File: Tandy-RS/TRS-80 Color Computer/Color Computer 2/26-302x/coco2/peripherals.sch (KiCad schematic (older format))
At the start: 0 parts

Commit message: -Added video sheet -moved salt chip from power sheet to peripheral sheet
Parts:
- added C11, C5: 100uF 16v, Capacitor_THT:CP_Radial_D8.0mm_P5.00mm, symbol Device:CP_Small
- added C2: 4700uF 16V, Capacitor_THT:CP_Radial_D16.0mm_P7.50mm, symbol Device:CP_Small
- added C6: .1uF, Capacitor_THT:C_Axial_L3.8mm_D2.6mm_P10.00mm_Horizontal, symbol Device:C_Small
- added J5: Conn_01x16_Female, Connector_PinHeader_2.54mm:PinHeader_1x15_P2.54mm_Vertical, symbol Connector:Conn_01x16_Female
- added Q1: 2N3055, Package_TO_SOT_THT:TO-3, symbol Transistor_BJT:2N3055
- added R1: 51, Resistor_THT:R_Axial_DIN0207_L6.3mm_D2.5mm_P10.16mm_Horizontal, symbol Device:R_Small_US
- added R2: .1 ohms 1/2W, Resistor_THT:R_Axial_DIN0411_L9.9mm_D3.6mm_P20.32mm_Horizontal, symbol Device:R_Small_US
- added U1: SC77527P, Package_DIP:DIP-16_W7.62mm, symbol coco2:SC77527P
- added U2: 6821, Package_DIP:DIP-40_W15.24mm, symbol Interface:6821
- added U3: SC77526, Package_DIP:DIP-20_W7.62mm, symbol custom_dac:SC77526
- added U7: 6822, Package_DIP:DIP-40_W15.24mm, symbol Interface:6822
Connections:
- new net: Q1.1 (B), U1.1 (PASS_TRANS_BASE_DRIVE)
- new net: Q1.2 (E), R1.1, R2.2
- new net: R1.2, U1.2 (PASS_TRANS_SENSE)
- new net: J5.9 (Pin_9), U7.10 (PB0)
- new net: J5.10 (Pin_10), U7.11 (PB1)
- new net: J5.11 (Pin_11), U7.12 (PB2)
- new net: J5.12 (Pin_12), U7.13 (PB3)
- new net: J5.13 (Pin_13), U7.14 (PB4)
- new net: J5.14 (Pin_14), U7.15 (PB5)
- new net: J5.15 (Pin_15), U7.16 (PB6)
- new net: J5.16 (Pin_16), U7.17 (PB7)
- new net: J5.1 (Pin_1), U7.2 (PA0)
- new net: J5.2 (Pin_2), U7.3 (PA1)
- new net: J5.3 (Pin_3), U7.4 (PA2)
- new net: J5.4 (Pin_4), U7.5 (PA3)
- new net: J5.5 (Pin_5), U7.6 (PA4)
- new net: J5.6 (Pin_6), U7.7 (PA5)
- new net: J5.7 (Pin_7), U7.8 (PA6)
- new net: J5.8 (Pin_8), U7.9 (PA7)
- new net +5V: C11.1, C5.1, C6.2, R2.1, U1.3 (CURRENT_LIMT), U7.20 (VCC)
- new net +SALT_VIN: U1.15 (UN_REG_-V_IN)
- new net -SALT_VIN: C2.1, Q1.3 (C), U1.16 (UN_REG_+V_IN)
- new net D0: U7.33 (D0)
- new net D1: U7.32 (D1)
- new net D2: U7.31 (D2)
- new net D3: U7.30 (D3)
- new net D4: U7.29 (D4)
- new net D5: U7.28 (D5)
- new net D6: U7.27 (D6)
- new net D7: U7.26 (D7)
- new net GNDS: C11.2, C2.2, C5.2, C6.1, U1.8 (GND), U7.1 (VSS)
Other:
- note added: "The SALT chip (Supply and Level Translator)"
- note added: "http://roust-it.dk/coco/coco2_service_manual.pdf"
- note added: "interface level translation, cassette read"
- note added: "is responsible for supply regulation, RS-232"
- note added: "operations, and driving the cassette relay."

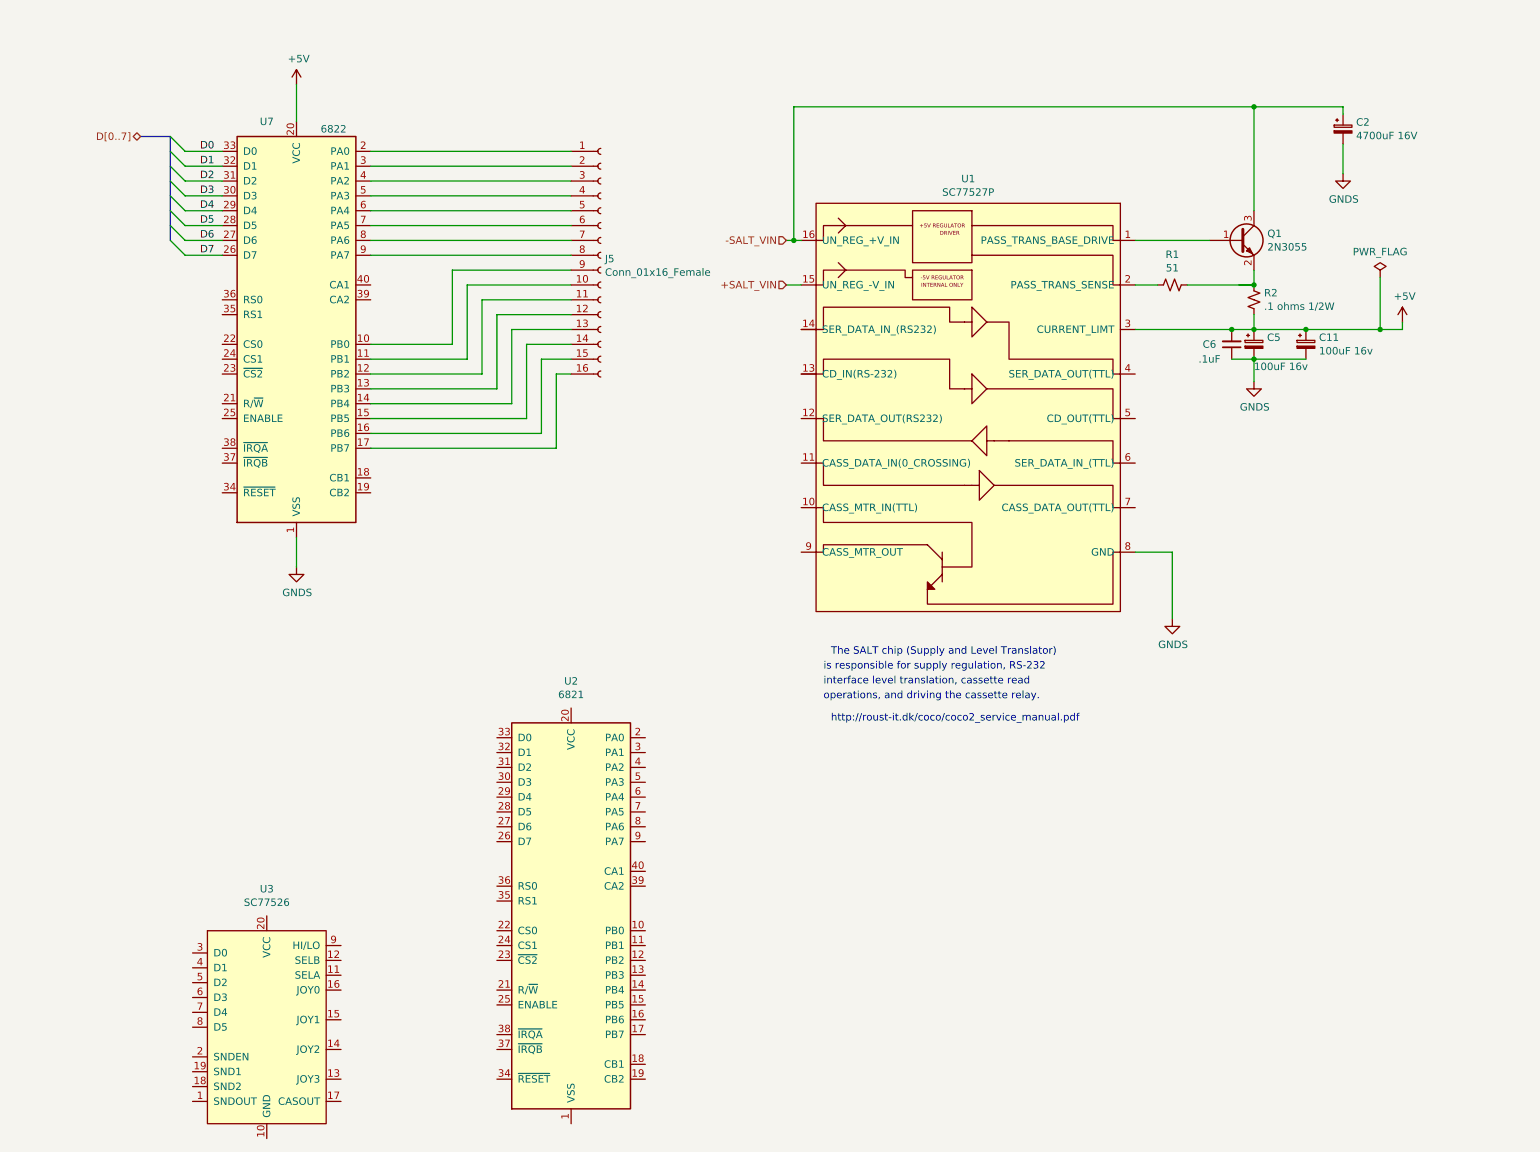
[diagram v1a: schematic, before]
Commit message: Added some more stuff to the perhipherals  sheet
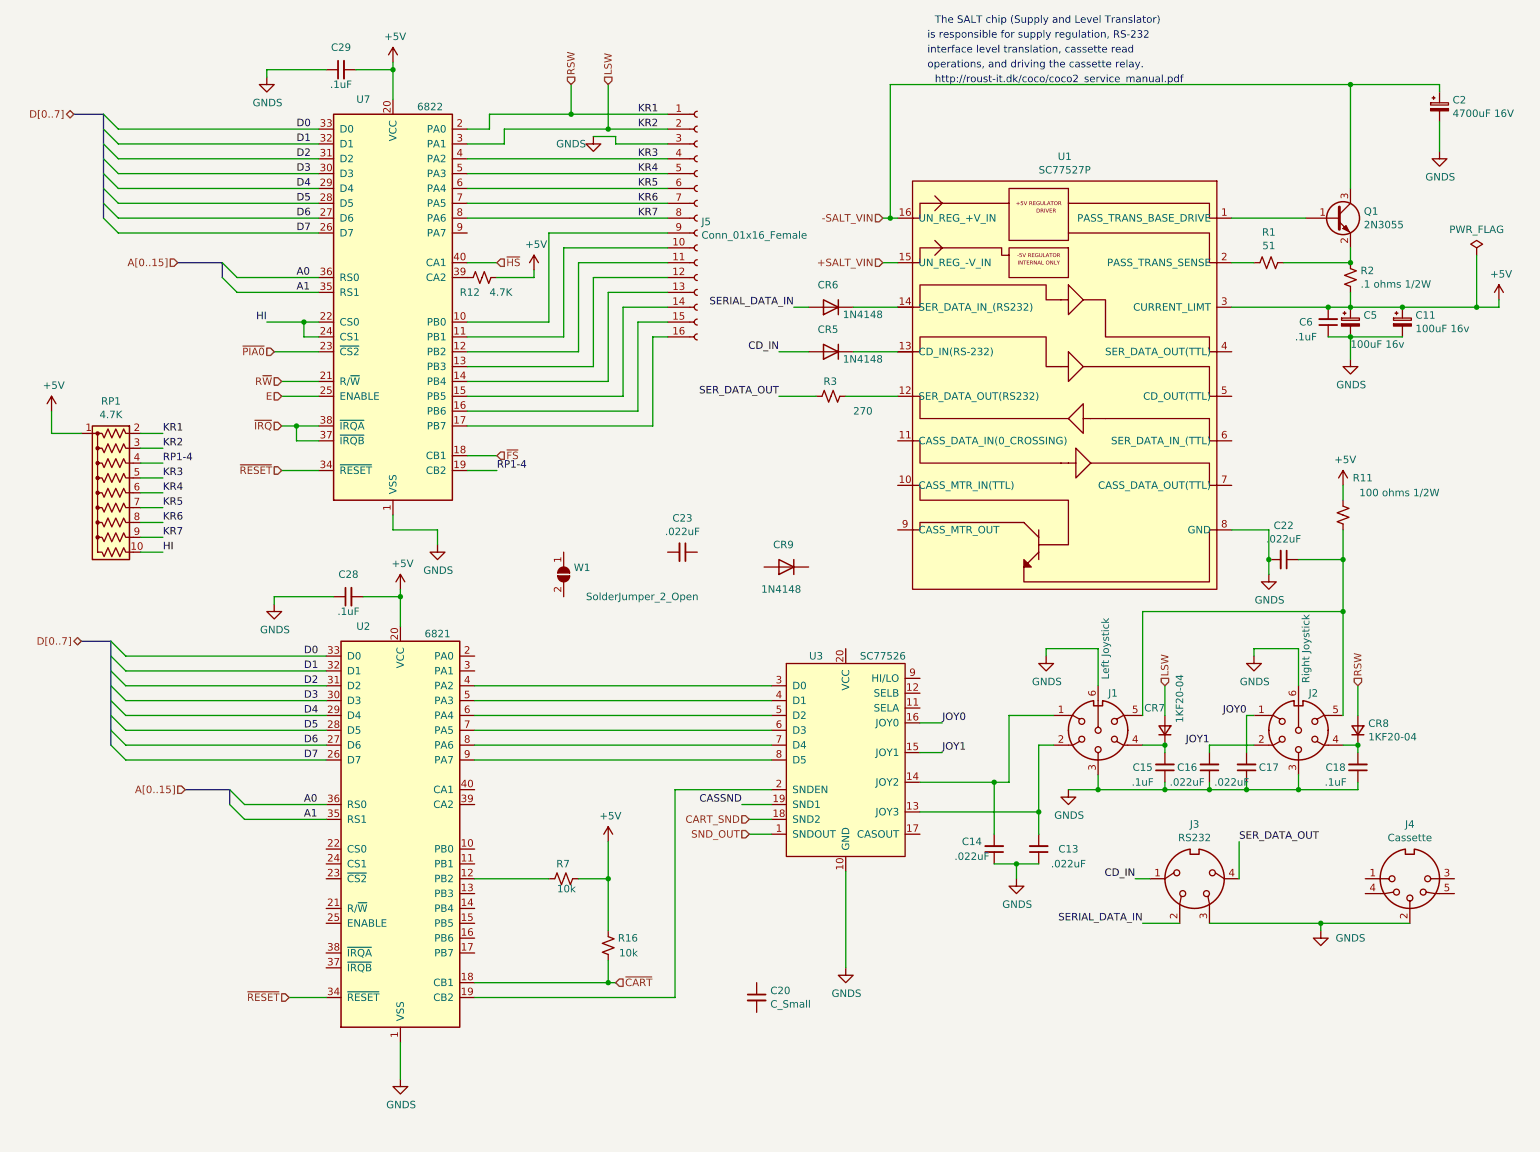
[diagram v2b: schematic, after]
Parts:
- added C13, C14, C16, C17, C22, C23: .022uF, Capacitor_THT:C_Disc_D8.0mm_W5.0mm_P5.00mm, symbol Device:C_Small
- added C15, C18, C28, C29: .1uF, Capacitor_THT:C_Axial_L3.8mm_D2.6mm_P10.00mm_Horizontal, symbol Device:C_Small
- added C20: C_Small, Capacitor_THT:CP_Radial_D5.0mm_P2.50mm, symbol Device:C_Small
- added CR5, CR6, CR9: 1N4148, Diode_THT:D_DO-35_SOD27_P7.62mm_Horizontal, symbol Diode:1N4148
- added CR7, CR8: 1KF20-04, Diode_THT:D_DO-15_P15.24mm_Horizontal, symbol Device:D_Small
- added J1: Left Joystick, coco2:CUI_SDS-60J, symbol Connector:DIN-6
- added J2: Right Joystick, coco2:CUI_SDS-60J, symbol Connector:DIN-6
- added J3: RS232, coco2:CUI_SDS-40J, symbol Connector:DIN-4
- added J4: Cassette, coco2:CUI_SDS-50J, symbol Connector:DIN-5_180degree
- added R11: 100 ohms 1/2W, Resistor_THT:R_Axial_DIN0411_L9.9mm_D3.6mm_P20.32mm_Horizontal, symbol Device:R_Small_US
- added R12: 4.7K, Resistor_THT:R_Axial_DIN0207_L6.3mm_D2.5mm_P10.16mm_Horizontal, symbol Device:R_Small_US
- added R16, R7: 10k, Resistor_THT:R_Axial_DIN0207_L6.3mm_D2.5mm_P10.16mm_Horizontal, symbol Device:R_Small_US
- added R3: 270, Resistor_THT:R_Axial_DIN0207_L6.3mm_D2.5mm_P10.16mm_Horizontal, symbol Device:R_Small_US
- added RP1: 4.7K, Resistor_THT:R_Array_SIP10, symbol Device:R_Network09_US
- added W1: SolderJumper_2_Open, Jumper:SolderJumper-2_P1.3mm_Open_RoundedPad1.0x1.5mm, symbol Jumper:SolderJumper_2_Open
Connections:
- net +5V: now also U2.20 (VCC), C28.2, C29.2, R11.1, R12.1, R16.2, R7.1, RP1.1 (common)
- net D0: now also U2.33 (D0)
- net D1: now also U2.32 (D1)
- net D2: now also U2.31 (D2)
- net D3: now also U2.30 (D3)
- net D4: now also U2.29 (D4)
- net D5: now also U2.28 (D5)
- net D6: now also U2.27 (D6)
- net D7: now also U2.26 (D7)
- net GNDS: now also J5.3 (Pin_3), U2.1 (VSS), U3.10 (GND), C13.1, C14.1, C15.1, C16.1, C17.1, C18.1, C22.2, C28.1, C29.1, J1.3, J1.6, J2.3, J2.6, J3.3, J4.2
- net at U1.12 (SER_DATA_OUT(RS232)): now also R3.1
- net at U1.13 (CD_IN(RS-232)): now also CR5.1 (K)
- net at U1.14 (SER_DATA_IN_(RS232)): now also CR6.1 (K)
- net at U2.12 (PB2): now also R7.2
- net ~CART: now reaches U2.18 (CB1)
- net ~CART: now also R16.1
- net at U2.19 (CB2): now also U3.2 (SNDEN)
- net ~RESET: now reaches U2.34 (~RESET)
- net ~RESET: now also U7.34 (~RESET)
- net A1: now reaches U2.35 (RS1)
- net A1: now also U7.35 (RS1)
- net A0: now reaches U2.36 (RS0)
- net A0: now also U7.36 (RS0)
- net at U2.4 (PA2): now also U3.3 (D0)
- net at U2.5 (PA3): now also U3.4 (D1)
- net at U2.6 (PA4): now also U3.5 (D2)
- net at U2.7 (PA5): now also U3.6 (D3)
- net at U2.8 (PA6): now also U3.7 (D4)
- net at U2.9 (PA7): now also U3.8 (D5)
- net SND_OUT: now reaches U3.1 (SNDOUT)
- net at U3.13 (JOY3): now also C13.2, J1.2
- net at U3.14 (JOY2): now also C14.2, J1.1
- net JOY1: now reaches U3.15 (JOY1)
- net JOY1: now also C16.2, J2.2
- net JOY0: now reaches U3.16 (JOY0)
- net JOY0: now also C17.2, J2.1
- net CART_SND: now reaches U3.18 (SND2)
- net CASSND: now reaches U3.19 (SND1)
- net ~FS: now reaches U7.18 (CB1)
- net RP1-4: now reaches U7.19 (CB2)
- net RP1-4: now also RP1.4 (R3)
- net RSW: now reaches J5.1 (Pin_1), U7.2 (PA0)
- net RSW: now also CR8.2 (A), RP1.2 (R1)
- net R~W: now reaches U7.21 (R/~W)
- net HI: now reaches U7.22 (CS0)
- net HI: now also U7.24 (CS1), RP1.10 (R9)
- net ~PIA0: now reaches U7.23 (~CS2)
- net E: now reaches U7.25 (ENABLE)
- net LSW: now reaches J5.2 (Pin_2), U7.3 (PA1)
- net LSW: now also CR7.2 (A), RP1.3 (R2)
- net ~IRQ: now reaches U7.37 (~IRQB)
- net ~IRQ: now also U7.38 (~IRQA)
- net at U7.39 (CA2): now also R12.2
- net KR3: now reaches U7.4 (PA2)
- net KR3: now also J5.4 (Pin_4), RP1.5 (R4); no longer J5.3 (Pin_3)
- net ~HS: now reaches U7.40 (CA1)
- net KR4: now reaches U7.5 (PA3)
- net KR4: now also J5.5 (Pin_5), RP1.6 (R5); no longer J5.4 (Pin_4)
- net KR5: now reaches U7.6 (PA4)
- net KR5: now also J5.6 (Pin_6), RP1.7 (R6); no longer J5.5 (Pin_5)
- net KR6: now reaches U7.7 (PA5)
- net KR6: now also J5.7 (Pin_7), RP1.8 (R7); no longer J5.6 (Pin_6)
- net KR7: now reaches U7.8 (PA6)
- net KR7: now also J5.8 (Pin_8), RP1.9 (R8); no longer J5.7 (Pin_7)
- net at U7.9 (PA7): no longer J5.8 (Pin_8)
- new net: C15.2, CR7.1 (K), J1.4
- new net: C22.1, J1.5, J2.5, R11.2
- new net: C18.2, CR8.1 (K), J2.4
- new net CD_IN: CR5.2 (A), J3.1
- new net SERIAL_DATA_IN: CR6.2 (A), J3.2
- new net SER_DATA_OUT: J3.4, R3.2
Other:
- moved on the sheet: C11, C2, C5, C6, J5, Q1, R1, R2, U1, U2, U3, U7

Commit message: Finished peripherals sheet. I think......
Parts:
- added C60: 33pF, Capacitor_THT:C_Rect_L7.2mm_W3.0mm_P5.00mm_FKS2_FKP2_MKS2_MKP2, symbol Device:C_Small
- added K1: HB1-DC5V-H62, coco2:HB1-DC5V-H62_W7.62mm, symbol coco2:HB1-DC5V-H62
- added R23: 220 1/2W, Resistor_THT:R_Axial_DIN0411_L9.9mm_D3.6mm_P20.32mm_Horizontal, symbol Device:R_Small_US
- added R4: 510, Resistor_THT:R_Axial_DIN0207_L6.3mm_D2.5mm_P10.16mm_Horizontal, symbol Device:R_Small_US
- added R8: 10k, Resistor_THT:R_Axial_DIN0207_L6.3mm_D2.5mm_P10.16mm_Horizontal, symbol Device:R_Small_US
- C20: value C_Small -> 10uF NP
- R11: value 100 ohms 1/2W -> 100 1/2W
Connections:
- net CASSND is gone; now on an unnamed net: U3.19 (SND1)
- net +5V: now also CR9.1 (K), R12.2, K1.2 (+); no longer R12.1
- net E: now also U2.25 (ENABLE), C60.2
- net GNDS: now also C23.1, C60.1, R23.1
- net HI: now also U2.22 (CS0), U2.24 (CS1)
- net RP1-4: now also U3.12 (SELB)
- net R~W: now also U2.21 (R/~W)
- net SND_OUT: now also R8.1
- net CASS_M_IN_TTL: now reaches U1.10 (CASS_MTR_IN(TTL))
- net CASS_M_IN_TTL: now also U2.39 (CA2)
- net at U1.11 (CASS_DATA_IN(0_CROSSING)): now also R4.2
- net SER_DATA_OUT_TTL: now reaches U1.4 (SER_DATA_OUT(TTL))
- net SER_DATA_OUT_TTL: now also U2.10 (PB0)
- net CD_OUT_TTL: now reaches U1.5 (CD_OUT(TTL))
- net CD_OUT_TTL: now also U2.40 (CA1)
- net SER_DATA_IN_TTL: now reaches U1.6 (SER_DATA_IN_(TTL))
- net SER_DATA_IN_TTL: now also U2.3 (PA1)
- net CASS_DATA_OUT_TTL: now reaches U1.7 (CASS_DATA_OUT(TTL))
- net CASS_DATA_OUT_TTL: now also U2.2 (PA0)
- net CASS_MTR_OUT: now reaches U1.9 (CASS_MTR_OUT)
- net CASS_MTR_OUT: now also CR9.2 (A), K1.8 (-)
- net at U2.11 (PB1): now also R8.2
- net at R7.2, U2.12 (PB2): now also W1.2 (B)
- net CSS: now reaches U2.13 (PB3)
- net ~INT~_EXT: now reaches U2.14 (PB4)
- net GM1: now reaches U2.15 (PB5)
- net GM2: now reaches U2.16 (PB6)
- net ~A~_G: now reaches U2.17 (PB7)
- net ~CS_PIA1: now reaches U2.23 (~CS2)
- net ~FIRQ: now reaches U2.37 (~IRQB)
- net ~FIRQ: now also U2.38 (~IRQA)
- net SELA: now reaches U3.11 (SELA)
- net SELA: now also R12.1, U7.39 (CA2)
- net CASSOUT: now reaches U3.17 (CASOUT)
- net CASSOUT: now also J4.5
- net HI_LO: now reaches U3.9 (HI/LO)
- net HI_LO: now also U7.9 (PA7)
- net at J5.15 (Pin_15), U7.16 (PB6): now also W1.1 (A)
- net CASS_DATA_IN: now reaches C20.1
- net CASS_DATA_IN: now also C23.2, J4.4, R23.2, R4.1
- net at J4.1: now also K1.14 (NO)
- net at J4.3: now also K1.9 (COM)
- net ~PIA0 renamed ~CS_PIA0
- no-connect marks 0 -> 1
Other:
- moved on the sheet: C20, C23, CR9, R12, RP1, W1
